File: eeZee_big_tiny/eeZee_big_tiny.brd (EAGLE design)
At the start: 17.7 x 45.2 mm, 10 parts, among them IC1 ATtiny2313

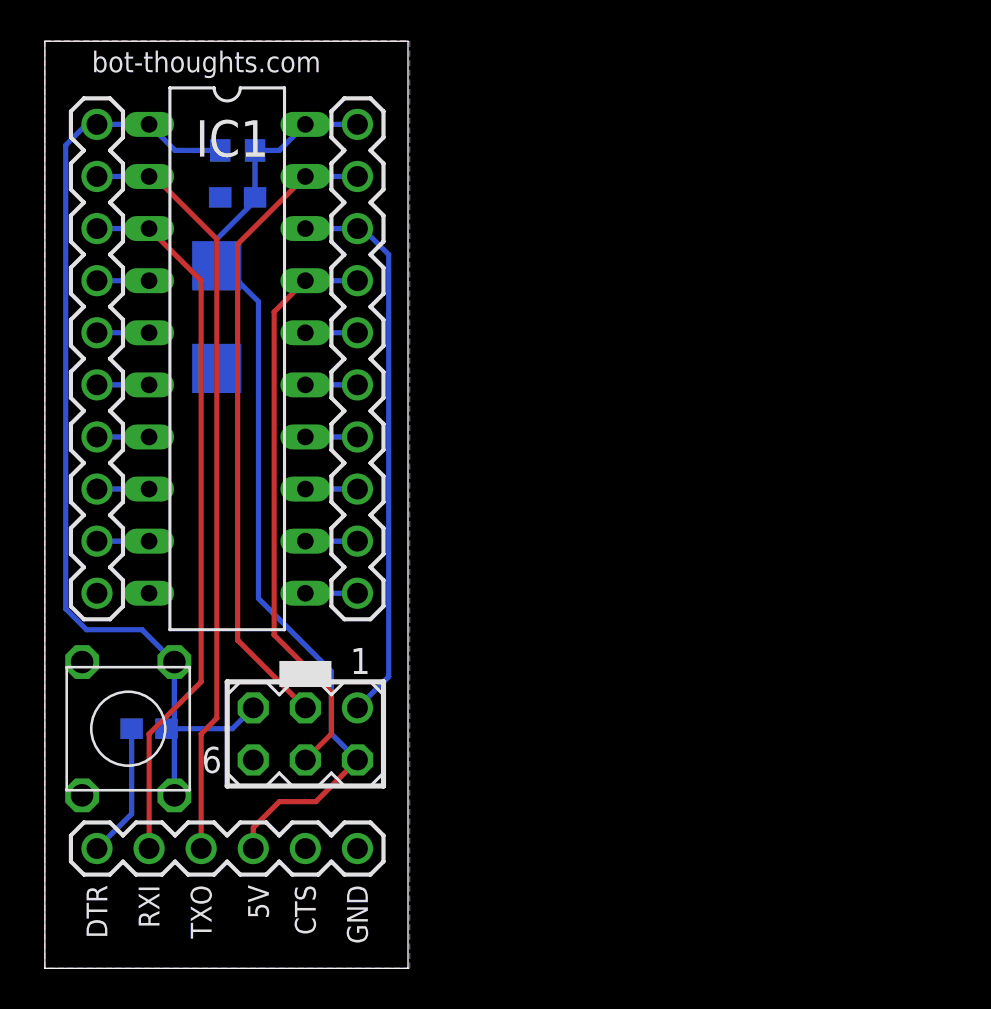
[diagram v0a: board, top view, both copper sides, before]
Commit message: Tweaks to big cap, routing
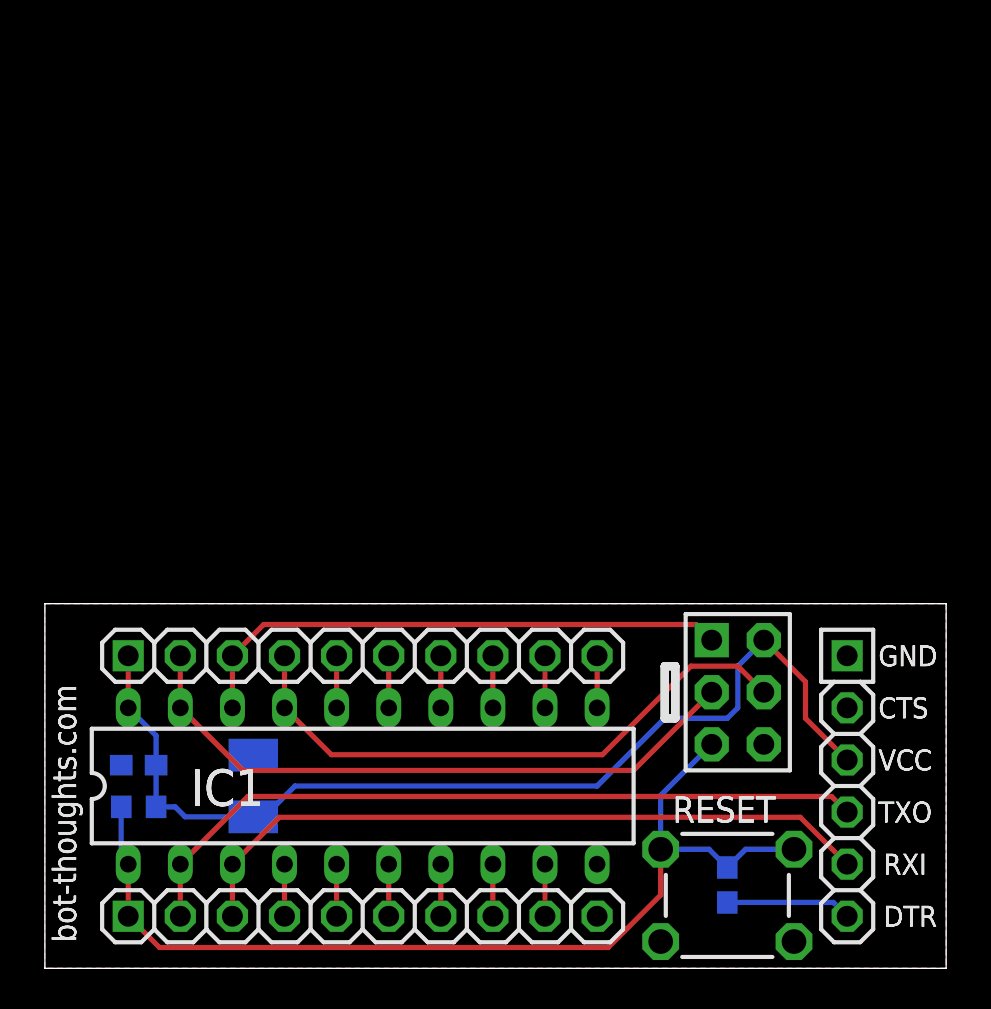
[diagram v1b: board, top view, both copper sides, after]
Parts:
- removed S1: (no value), mes_electromech:6MMTACTILE_4PIN
- removed SV1: (no value), con-lstb:MA03-2
- added J2: avrisp, ads4:CON6P2R
- added S2: RESET, mes_electromech:6MMTACTILE_4PIN
- C2: device rcl:SMC_C -> rcl:SMC_B
- IC1: value ATtiny2313 -> TINY2313-*P*; device avr:DIL20 -> avr-7:DIL20
- JP1: value (none) -> FTDI; device SparkFun:1X10 -> pinhead-2:1X06-S
- JP2: device SparkFun:1X10 -> pinhead-2:1X10-S
- JP3: value FTDI -> (none); device SparkFun:1X06 -> pinhead-2:1X10-S
- moved JP1 40.1 mm to (39.1, 8.89)
- moved R1 32.4 mm to (4.57, 7.87)
- moved C3 29.2 mm to (33.3, 4.06), turned to 270 degrees
- moved C1 28.1 mm to (4.57, 9.91)
- moved C2 22.9 mm to (10.2, 8.89), turned to 90 degrees
- moved IC1 21.8 mm to (15.5, 8.89), turned to 0 degrees
- moved JP2 13.3 mm to (15.5, 15.2), turned to 0 degrees
- moved JP3 3.31 mm to (15.5, 2.54), turned to 0 degrees
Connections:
- removed net MISO: IC1.18, JP1.3, SV1.1
- removed net MOSI: IC1.17, JP1.4, SV1.4
- removed net N$1: C3.2, JP3.6
- removed net N$16: IC1.7, JP2.4
- removed net N$17: IC1.6, JP2.5
- removed net N$18: IC1.3, JP2.8, JP3.5
- removed net RX: IC1.2, JP2.9, JP3.4
- removed net SCK: IC1.19, JP1.2, SV1.3
- new net DTR: C3.2, JP1.6
- new net N$4: IC1.19, J2.3, JP2.2
- new net N$6: IC1.6, JP3.6
- new net N$7: IC1.7, JP3.7
- new net RXI: IC1.3, JP1.5, JP3.3
- new net TXO: IC1.2, JP1.4, JP3.2
- new net XTAL1: IC1.5, JP3.5
- new net XTAL2: IC1.4, JP3.4
- net !RESET: now also J2.5, JP3.1, S2.B1, S2.B2; no longer JP2.10, S1.A1, S1.A2, SV1.5
- net GND: now also J2.6, JP1.1, JP3.10, S2.A1, S2.A2; no longer JP2.1, JP3.1, S1.B1, S1.B2, SV1.6
- net N$10: now also IC1.11, JP2.10; no longer IC1.14, JP1.7
- net N$11: now also IC1.12, JP2.9; no longer IC1.13, JP1.8
- net N$12: now also IC1.13, JP2.8; no longer IC1.12, JP1.9
- net N$13: now also IC1.14, JP2.7; no longer IC1.11, JP1.10
- net N$14: now also IC1.15, JP2.6; no longer IC1.9, JP2.2
- net N$15: now also IC1.16, JP2.5; no longer IC1.8, JP2.3
- net N$2: now also IC1.18, J2.1, JP2.3; no longer IC1.4, JP2.7
- net N$3: now also IC1.17, J2.4, JP2.4; no longer IC1.5, JP2.6
- net N$8: now also IC1.8, JP3.8; no longer IC1.16, JP1.5
- net N$9: now also IC1.9, JP3.9; no longer IC1.15, JP1.6
- net VCC: now also J2.2, JP1.3, JP2.1; no longer JP1.1, JP3.3, SV1.2
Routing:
- net RX: track 37.1 -> 0.00 mm
- net TXO: track 0.00 -> 36.7 mm
- net N$18: track 34.9 -> 0.00 mm
- net RXI: track 0.00 -> 34.4 mm
- net N$4: track 0.00 -> 31.3 mm
- net SCK: track 31.2 -> 0.00 mm
- net MOSI: track 28.2 -> 0.00 mm
- net MISO: track 27.3 -> 0.00 mm
- net N$3: track 2.54 -> 29.2 mm
- net N$2: track 2.54 -> 26.9 mm
- net N$1: track 6.54 -> 0.00 mm
- net DTR: track 0.00 -> 6.12 mm
- net VCC: track 46.4 -> 50.0 mm
- net XTAL2: track 0.00 -> 2.54 mm
- net XTAL1: track 0.00 -> 2.54 mm
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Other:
- board size 17.7 x 45.2 mm -> 43.9 x 17.8 mm
- board text added: "C1"
- board text added: "C2"
- board text added: "C3"
- board text added: "IC1"
- board text added: "R1"
- board text added: "RESET"
- board text added: "Rev 0.1"
- board text added: "VCC"
- board text added: "eeZee Big Tiny"
- board text removed: "5V"

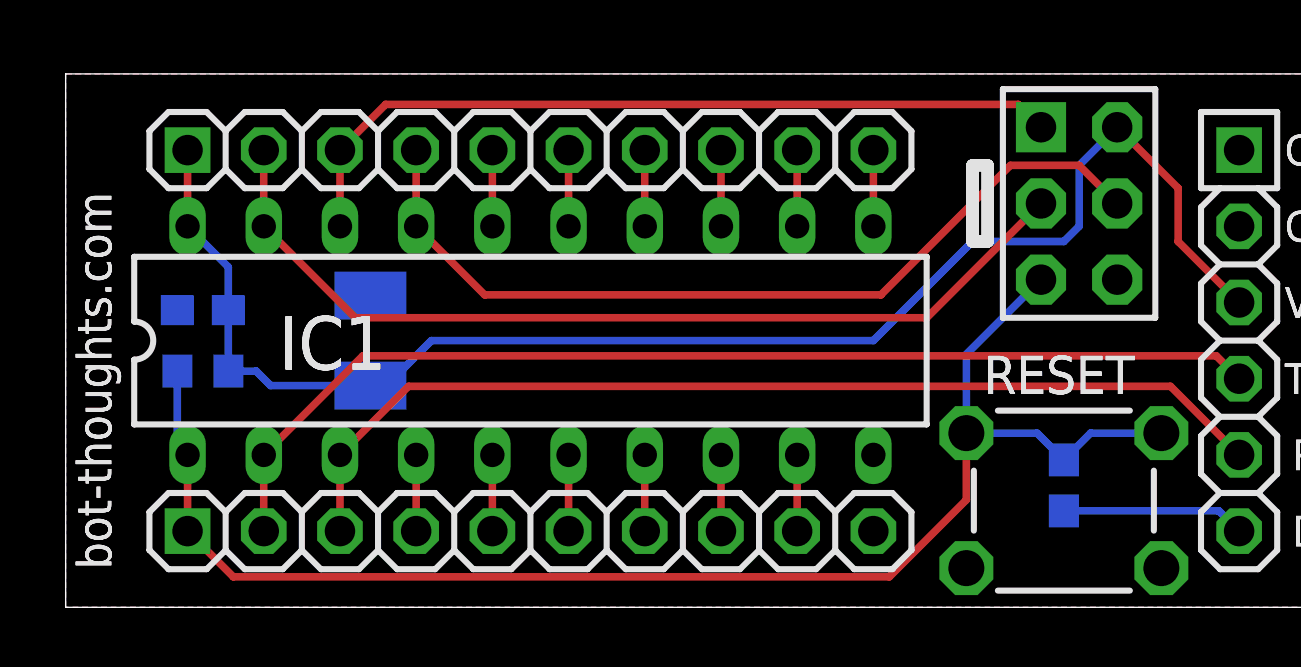
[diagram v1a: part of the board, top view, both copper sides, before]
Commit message: Added crystal+caps
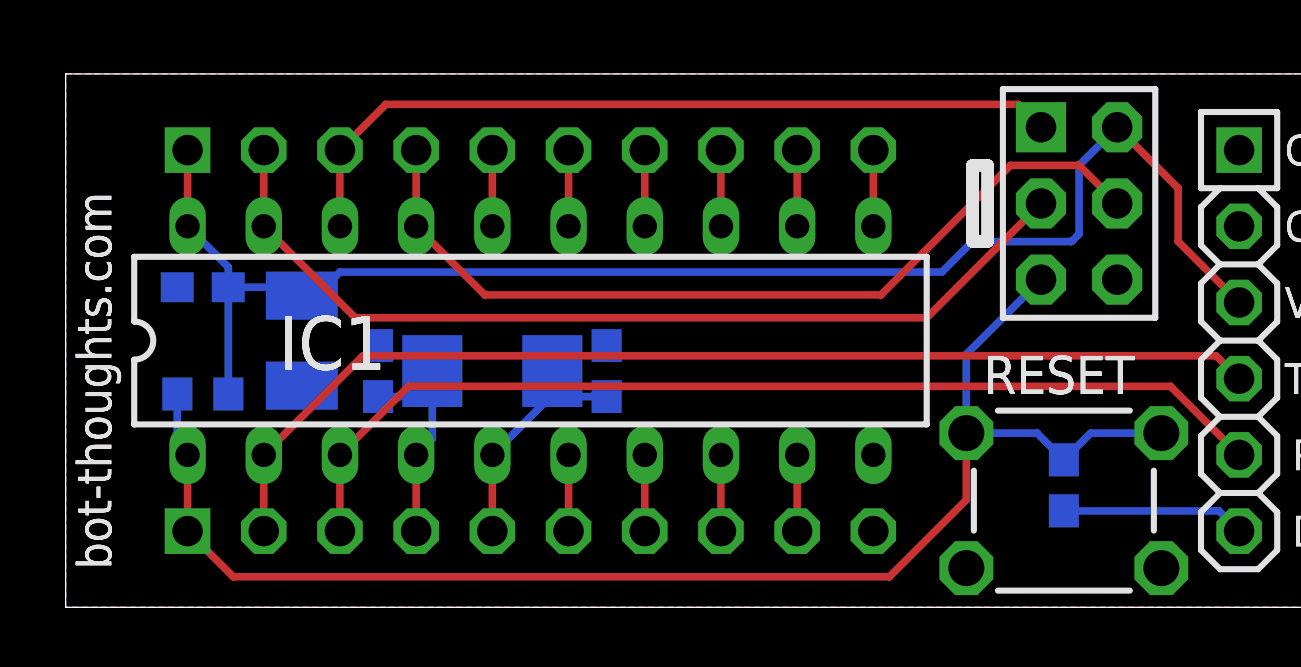
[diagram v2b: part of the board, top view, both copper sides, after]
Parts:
- added C4, C5: 8pF, rcl:C0603
- added Q1: 16MHz, mes_crystal:NDK_2PAD_5X3
- moved C2 2.29 mm to (7.87, 8.89), turned to 270 degrees
- moved R1 0.76 mm to (4.57, 7.11)
- moved C1 0.76 mm to (4.57, 10.7)
- flipped JP2 to the bottom, turned to 180 degrees
- flipped JP3 to the bottom, turned to 180 degrees
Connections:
- net GND: now also C4.2, C5.2
- net XTAL1: now also C5.1, Q1.P$1
- net XTAL2: now also C4.1, Q1.P$2
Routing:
- net XTAL1: track 2.54 -> 8.32 mm
- net XTAL2: track 2.54 -> 7.72 mm
- net !RESET: track 48.7 -> 48.0 mm

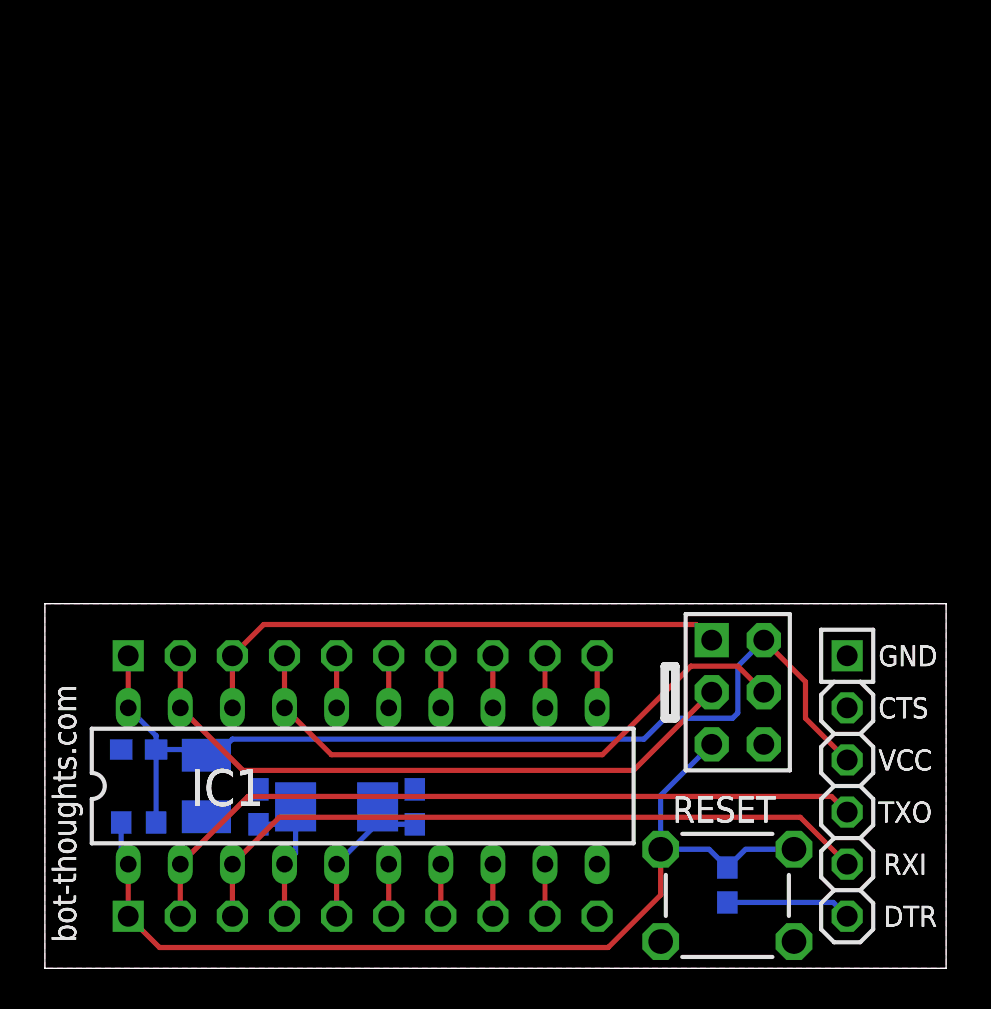
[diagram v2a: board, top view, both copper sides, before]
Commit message: Removed FTDI header, revised layout to reduce leading edge clearance on breadboard.
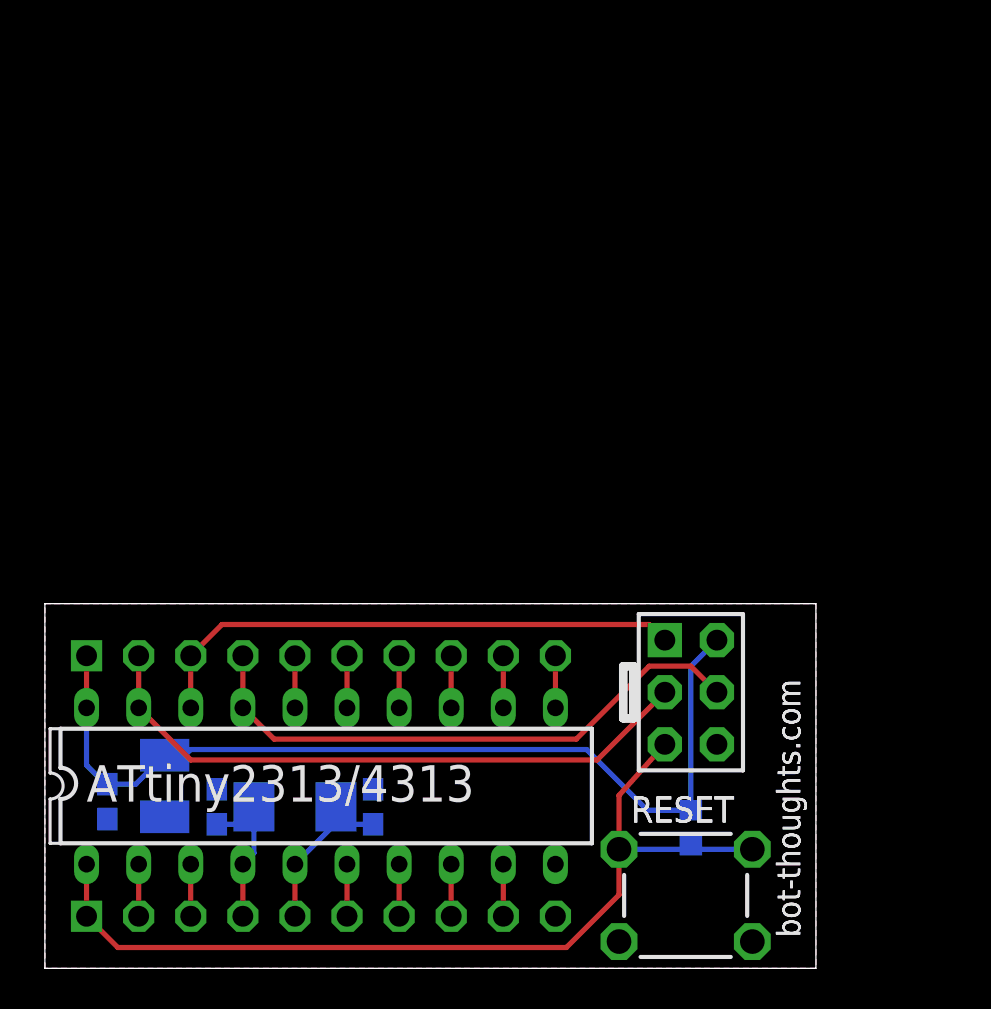
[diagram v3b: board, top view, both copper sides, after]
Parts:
- removed C3: 0.1uF, rcl:C0603
- removed JP1: FTDI, pinhead-2:1X06-S
- IC1: value TINY2313-*P* -> ATtiny2313/4313
- moved R1 26.9 mm to (31.5, 6.86), turned to 90 degrees
- moved C1 2.96 mm to (3.05, 8.13), turned to 270 degrees
- moved J2 2.29 mm to (31.5, 13.5)
- moved C2 2.03 mm to (5.84, 8.89)
- moved C4 2.03 mm to (8.38, 7.87)
- moved C5 2.03 mm to (16.0, 7.87)
- moved IC1 2.03 mm to (13.5, 8.89)
- moved JP2 2.03 mm to (13.5, 15.2)
- moved JP3 2.03 mm to (13.5, 2.54)
- moved Q1 2.03 mm to (12.2, 7.87)
- moved S2 2.03 mm to (31.2, 3.56)
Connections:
- removed net DTR: C3.2, JP1.6
- net !RESET: no longer C3.1
- net GND: no longer JP1.1
- net RXI: no longer JP1.5
- net TXO: no longer JP1.4
- net VCC: no longer JP1.3
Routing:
- net TXO: track 36.7 -> 2.54 mm
- net RXI: track 34.4 -> 2.54 mm
- net DTR: track 6.12 -> 0.00 mm
- net VCC: track 49.6 -> 45.9 mm
- net !RESET: track 48.0 -> 45.1 mm
- net N$3: track 29.2 -> 28.3 mm
- net N$4: track 31.3 -> 30.6 mm
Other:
- board size 43.9 x 17.8 mm -> 37.6 x 17.8 mm
- board text added: "16MHz"
- board text added: "ATtiny2313/4313"
- board text added: "C4"
- board text added: "C5"
- board text removed: "C3"
- board text removed: "CTS"
- board text removed: "DTR"
- board text removed: "GND"
- board text removed: "IC1"
- board text removed: "RXI"
- board text removed: "TXO"
- board text removed: "VCC"
- board text removed: "eeZee Big Tiny"

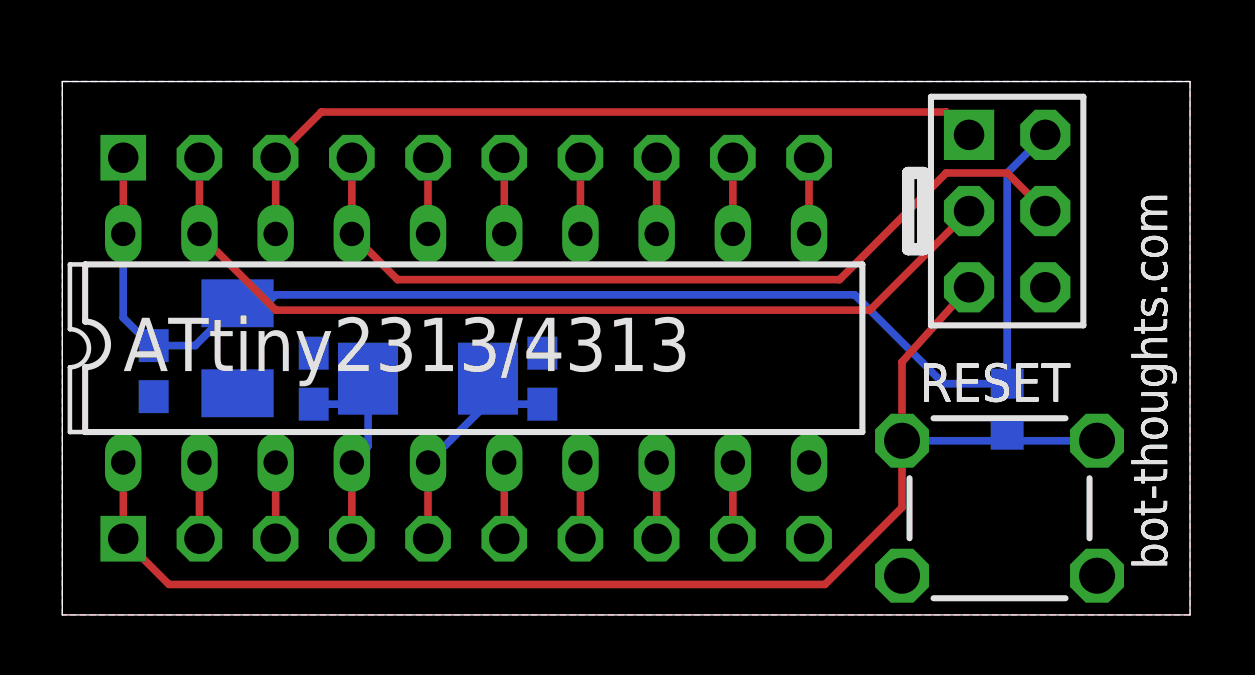
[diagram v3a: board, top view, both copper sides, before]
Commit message: Revised board layout to match the new Tiny style, swapping in new reset button
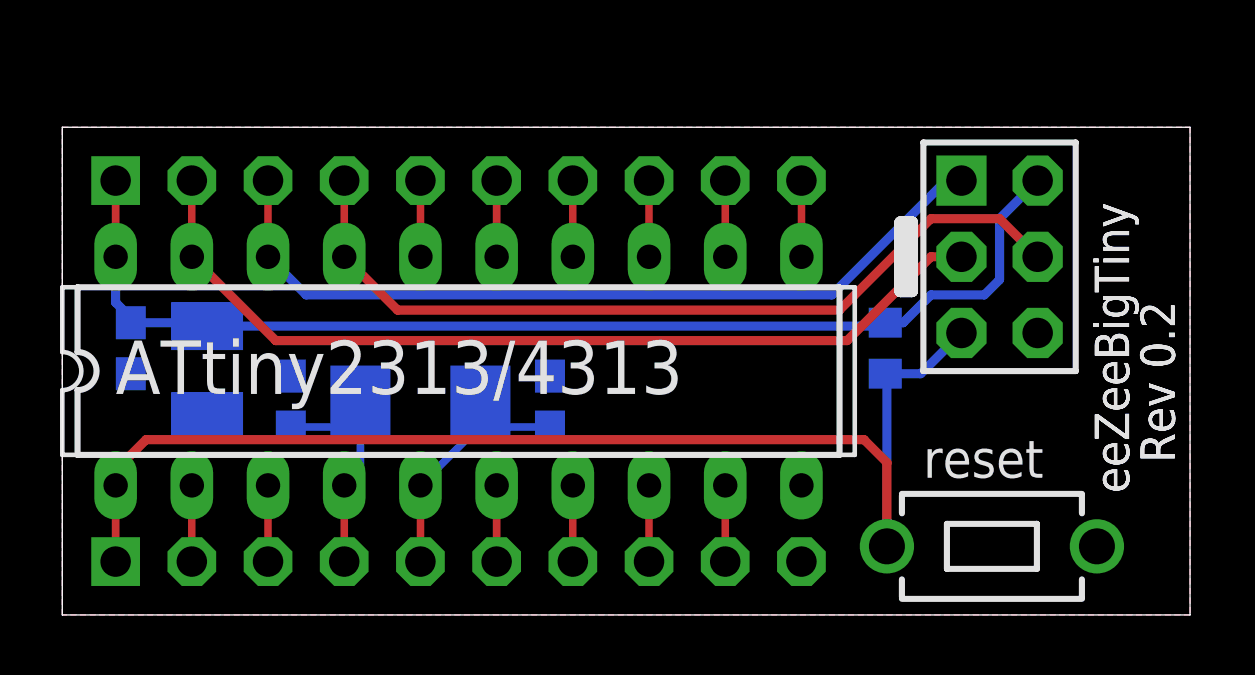
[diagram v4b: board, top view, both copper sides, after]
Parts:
- removed S2: RESET, mes_electromech:6MMTACTILE_4PIN
- added S1: reset, mes_electromech:6MMTACTILE_RECT
- moved R1 4.54 mm to (27.4, 8.89)
- moved J2 1.55 mm to (31.2, 11.9)
- moved C2 1.27 mm to (4.83, 8.13)
- moved C1 1.08 mm to (2.29, 8.89)
- moved C4 1.08 mm to (7.62, 7.11)
- moved IC1 0.80 mm to (13.2, 8.13)
- moved JP2 0.80 mm to (13.2, 14.5)
- moved C5 0.80 mm to (16.3, 7.11)
- moved JP3 0.80 mm to (13.2, 1.78)
- moved Q1 0.80 mm to (11.9, 7.11)
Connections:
- net !RESET: now also S1.P$2; no longer S2.B1, S2.B2
- net GND: now also S1.P$1; no longer S2.A1, S2.A2
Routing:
- net VCC: track 45.9 -> 38.7 mm
- net !RESET: track 45.1 -> 41.2 mm
- net N$2: track 26.6 -> 27.8 mm
- net XTAL1: track 8.32 -> 8.83 mm
- net XTAL2: track 7.72 -> 8.23 mm
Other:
- board size 37.6 x 17.8 mm -> 37.6 x 16.3 mm
- board text added: "Rev 0.2"
- board text added: "eeZeeBigTiny"
- board text added: "reset"
- board text removed: "RESET"
- board text removed: "Rev 0.1"
